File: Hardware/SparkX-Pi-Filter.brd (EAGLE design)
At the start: 25.4 x 25.4 mm, 19 parts

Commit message: Added Pi to 100 Digits
Added silk on back of board with Pi to 100 digits
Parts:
- added U$10: (no value), buzzard_labels_pi:50288419713
- added U$11: (no value), buzzard_labels_pi:69399375104
- added U$12: (no value), buzzard_labels_pi:58209749445
- added U$13: (no value), buzzard_labels_pi:59230781646
- added U$14: (no value), buzzard_labels_pi:06286208997
- added U$15: (no value), buzzard_labels_pi:86280348258
- added U$16: (no value), buzzard_labels_pi:34211706799
- added U$7: (no value), buzzard_labels_pi:3#4159265350
- added U$8: (no value), buzzard_labels_pi:89793238461
- added U$9: (no value), buzzard_labels_pi:26433832792
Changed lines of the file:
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@@
 <element name="U$5" library="buzzard_labels_v01" package="VIN1" value="" x="1.27" y="17.78" smashed="yes"/>
 <element name="U$6" library="buzzard_labels_v01" package="VOUT2" value="" x="19.05" y="17.78" smashed="yes"/>
+<element name="U$7" library="buzzard_labels_pi" package="3#4159265350" value="" x="17.78" y="24.13" smashed="yes" rot="MR0"/>
+<element name="U$8" library="buzzard_labels_pi" package="89793238461" value="" x="17.78" y="21.59" smashed="yes" rot="MR0"/>
+<element name="U$9" library="buzzard_labels_pi" package="26433832792" value="" x="17.78" y="19.05" smashed="yes" rot="MR0"/>
+<element name="U$10" library="buzzard_labels_pi" package="50288419713" value="" x="17.78" y="16.51" smashed="yes" rot="MR0"/>
+<element name="U$11" library="buzzard_labels_pi" package="69399375104" value="" x="17.78" y="13.97" smashed="yes" rot="MR0"/>
+<element name="U$12" library="buzzard_labels_pi" package="58209749445" value="" x="17.78" y="11.43" smashed="yes" rot="MR0"/>
+<element name="U$13" library="buzzard_labels_pi" package="59230781646" value="" x="17.78" y="8.89" smashed="yes" rot="MR0"/>
+<element name="U$14" library="buzzard_labels_pi" package="06286208997" value="" x="17.78" y="6.35" smashed="yes" rot="MR0"/>
+<element name="U$15" library="buzzard_labels_pi" package="86280348258" value="" x="17.78" y="3.81" smashed="yes" rot="MR0"/>
+<element name="U$16" library="buzzard_labels_pi" package="34211706799" value="" x="17.78" y="1.27" smashed="yes" rot="MR0"/>
 </elements>
 <signals>

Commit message: Changed Buzzard label for pi numbers to text
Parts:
- removed U$13: (no value), buzzard_labels_pi:59230781646
- removed U$14: (no value), buzzard_labels_pi:06286208997
- removed U$15: (no value), buzzard_labels_pi:86280348258
- removed U$16: (no value), buzzard_labels_pi:34211706799
- U$10: device buzzard_labels_pi:50288419713 -> buzzard_labels_pi_plaintext:0938446095_5058223172_53594081284
- U$11: device buzzard_labels_pi:69399375104 -> buzzard_labels_pi_plaintext:4811174502_8410270193_85211055595
- U$12: device buzzard_labels_pi:58209749445 -> buzzard_labels_pi_plaintext:6446229489_5493038196_44288109756
- U$6: device buzzard_labels_v01:VOUT2 -> buzzard_labels_pi_plaintext:3#1415926535__8979323846_26433832790
- U$7: device buzzard_labels_pi:3#4159265350 -> buzzard_labels_pi_plaintext:5028841971_6939937510_58209749441
- U$8: device buzzard_labels_pi:89793238461 -> buzzard_labels_pi_plaintext:5923078164_0628620899_86280348252
- U$9: device buzzard_labels_pi:26433832792 -> buzzard_labels_pi_plaintext:3421170679_8214808651_32823066473
- moved U$9 8.08 mm to (23.4, 13.2)
- moved U$11 7.74 mm to (22.9, 8.13)
- moved U$7 7.65 mm to (23.5, 19.1)
- moved U$10 7.22 mm to (23.4, 11.9)
- moved U$12 6.83 mm to (22.9, 6.86)
- moved U$8 6.76 mm to (23.4, 17.8)
- moved U$6 6.02 mm to (24.5, 20.3), flipped to the bottom
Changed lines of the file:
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@@
 <setting verticaltext="up"/>
 </settings>
-<grid distance="0.05" unitdist="inch" unit="inch" style="lines" multiple="1" display="yes" altdistance="0.005" altunitdist="inch" altunit="inch"/>
+<grid distance="0.01" unitdist="inch" unit="inch" style="lines" multiple="1" display="yes" altdistance="0.001" altunitdist="inch" altunit="inch"/>
 <layers>
 <layer number="1" name="Top" color="4" fill="1" visible="yes" active="yes"/>
@@
 <element name="U$4" library="buzzard_labels_v01" package="PI#FILTER3" value="" x="8.89" y="20.32" smashed="yes"/>
 <element name="U$5" library="buzzard_labels_v01" package="VIN1" value="" x="1.27" y="17.78" smashed="yes"/>
-<element name="U$6" library="buzzard_labels_v01" package="VOUT2" value="" x="19.05" y="17.78" smashed="yes"/>
-<element name="U$7" library="buzzard_labels_pi" package="3#4159265350" value="" x="17.78" y="24.13" smashed="yes" rot="MR0"/>
-<element name="U$8" library="buzzard_labels_pi" package="89793238461" value="" x="17.78" y="21.59" smashed="yes" rot="MR0"/>
-<element name="U$9" library="buzzard_labels_pi" package="26433832792" value="" x="17.78" y="19.05" smashed="yes" rot="MR0"/>
-<element name="U$10" library="buzzard_labels_pi" package="50288419713" value="" x="17.78" y="16.51" smashed="yes" rot="MR0"/>
-<element name="U$11" library="buzzard_labels_pi" package="69399375104" value="" x="17.78" y="13.97" smashed="yes" rot="MR0"/>
-<element name="U$12" library="buzzard_labels_pi" package="58209749445" value="" x="17.78" y="11.43" smashed="yes" rot="MR0"/>
-<element name="U$13" library="buzzard_labels_pi" package="59230781646" value="" x="17.78" y="8.89" smashed="yes" rot="MR0"/>
-<element name="U$14" library="buzzard_labels_pi" package="06286208997" value="" x="17.78" y="6.35" smashed="yes" rot="MR0"/>
-<element name="U$15" library="buzzard_labels_pi" package="86280348258" value="" x="17.78" y="3.81" smashed="yes" rot="MR0"/>
-<element name="U$16" library="buzzard_labels_pi" package="34211706799" value="" x="17.78" y="1.27" smashed="yes" rot="MR0"/>
+<element name="U$6" library="buzzard_labels_pi_plaintext" package="3#1415926535__8979323846_26433832790" value="" x="24.511" y="20.32" smashed="yes" rot="MR0"/>
+<element name="U$7" library="buzzard_labels_pi_plaintext" package="5028841971_6939937510_58209749441" value="" x="23.495" y="19.05" smashed="yes" rot="MR0"/>
+<element name="U$8" library="buzzard_labels_pi_plaintext" package="5923078164_0628620899_86280348252" value="" x="23.368" y="17.78" smashed="yes" rot="MR0"/>
+<element name="U$9" library="buzzard_labels_pi_plaintext" package="3421170679_8214808651_32823066473" value="" x="23.368" y="13.208" smashed="yes" rot="MR0"/>
+<element name="U$10" library="buzzard_labels_pi_plaintext" package="0938446095_5058223172_53594081284" value="" x="23.368" y="11.938" smashed="yes" rot="MR0"/>
+<element name="U$11" library="buzzard_labels_pi_plaintext" package="4811174502_8410270193_85211055595" value="" x="22.86" y="8.128" smashed="yes" rot="MR0"/>
+<element name="U$12" library="buzzard_labels_pi_plaintext" package="6446229489_5493038196_44288109756" value="" x="22.86" y="6.858" smashed="yes" rot="MR0"/>
 </elements>
 <signals>

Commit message: Updated to meet standards
Fixed width edge, added labels for C1, L1, C2 and Vout.  Added version.
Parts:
- added U$13: (no value), buzzard_labels_v01:VOUT2
- added U$14: (no value), buzzard_refdes_v01:C10
- added U$15: (no value), buzzard_refdes_v01:C21
- added U$16: (no value), buzzard_refdes_v01:L12
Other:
- board text added: "x01"
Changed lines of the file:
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@@
 <board>
 <plain>
-<wire x1="0" y1="0" x2="25.4" y2="0" width="0" layer="20"/>
-<wire x1="25.4" y1="0" x2="25.4" y2="25.4" width="0" layer="20"/>
-<wire x1="25.4" y1="25.4" x2="0" y2="25.4" width="0" layer="20"/>
-<wire x1="0" y1="25.4" x2="0" y2="0" width="0" layer="20"/>
+<wire x1="0" y1="0" x2="25.4" y2="0" width="0.2032" layer="20"/>
+<wire x1="25.4" y1="0" x2="25.4" y2="25.4" width="0.2032" layer="20"/>
+<wire x1="25.4" y1="25.4" x2="0" y2="25.4" width="0.2032" layer="20"/>
+<wire x1="0" y1="25.4" x2="0" y2="0" width="0.2032" layer="20"/>
 <text x="19.05" y="-17.78" size="1.778" layer="51" font="vector" ratio="15">The Hoff</text>
+<text x="9.144" y="1.016" size="1.778" layer="16" rot="MR0">x01</text>
 </plain>
 <attributes>
@@
 <element name="U$11" library="buzzard_labels_pi_plaintext" package="4811174502_8410270193_85211055595" value="" x="22.86" y="8.128" smashed="yes" rot="MR0"/>
 <element name="U$12" library="buzzard_labels_pi_plaintext" package="6446229489_5493038196_44288109756" value="" x="22.86" y="6.858" smashed="yes" rot="MR0"/>
+<element name="U$13" library="buzzard_labels_v01" package="VOUT2" value="" x="18.796" y="17.526" smashed="yes"/>
+<element name="U$14" library="buzzard_refdes_v01" package="C10" value="" x="3.556" y="12.7" smashed="yes"/>
+<element name="U$15" library="buzzard_refdes_v01" package="C21" value="" x="18.796" y="12.7" smashed="yes"/>
+<element name="U$16" library="buzzard_refdes_v01" package="L12" value="" x="11.176" y="17.018" smashed="yes"/>
 </elements>
 <signals>

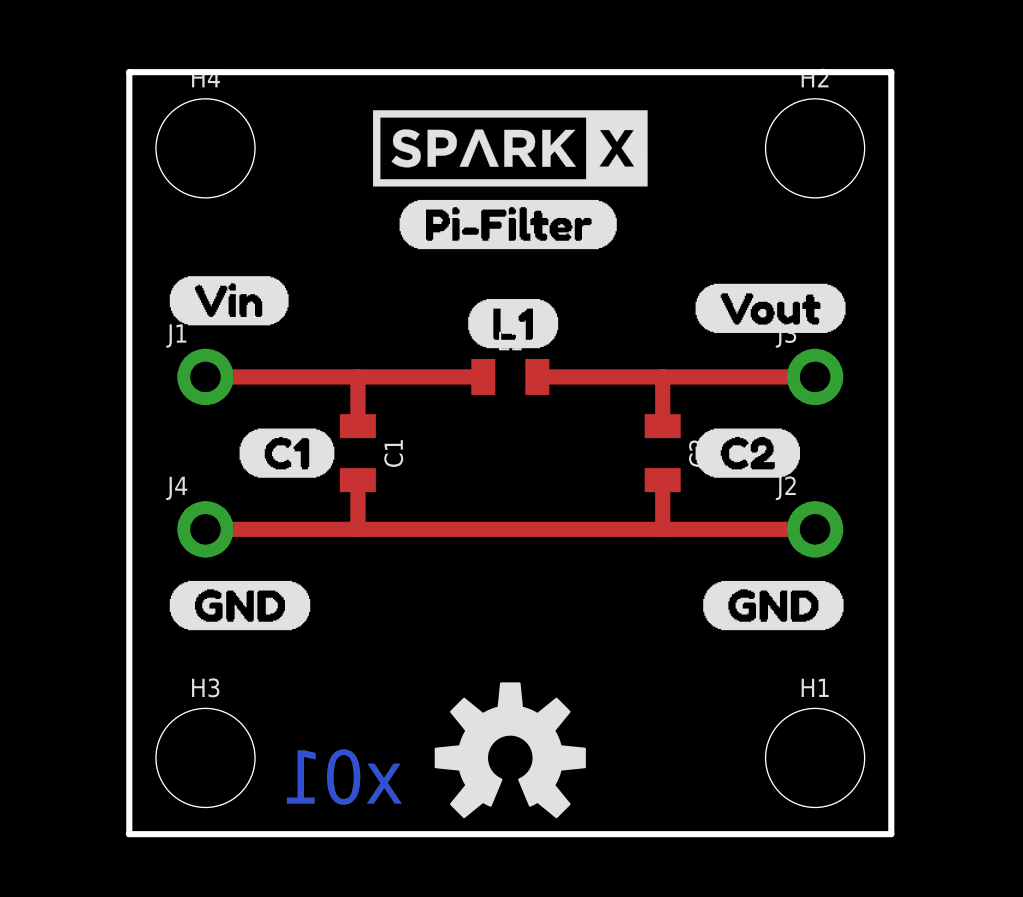
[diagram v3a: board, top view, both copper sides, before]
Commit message: Added Screw Terminals and adjusted labels
Added Screw Terminals and adjusted labels
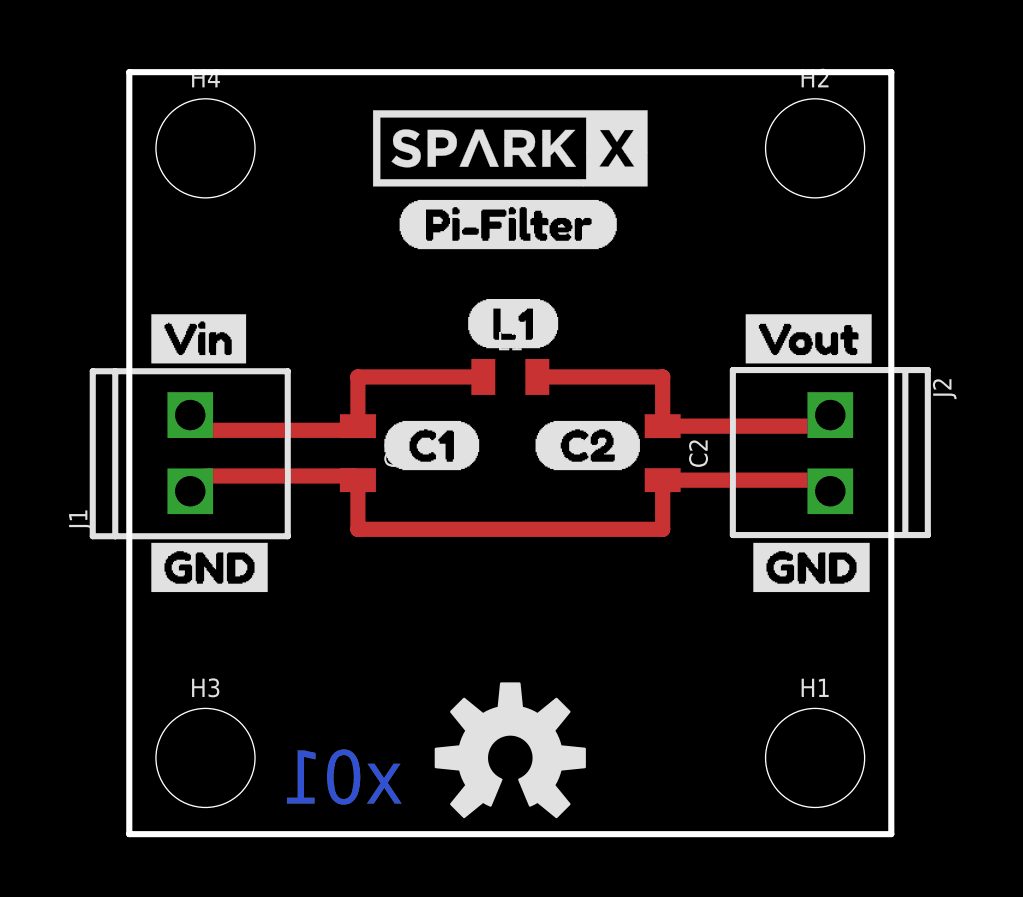
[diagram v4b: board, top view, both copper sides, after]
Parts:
- removed J3, J4: (no value), SparkFun-Connectors:1X01_NO_SILK
- J1, J2: device SparkFun-Connectors:1X01_NO_SILK -> SparkFun-Connectors:1X02_2.54_SCREWTERM
- U$13: device buzzard_labels_v01:VOUT2 -> buzzard_labels_v02:VOUT2
- U$2, U$3: device buzzard_labels_v01:GND0 -> buzzard_labels_v02:GND0
- U$5: device buzzard_labels_v01:VIN1 -> buzzard_labels_v02:VIN1
- moved U$2 19.1 mm to (20.3, 8.89)
- moved U$3 18.8 mm to (0.25, 8.89)
- moved U$15 5.34 mm to (13.5, 13.0)
- moved U$14 4.83 mm to (8.38, 13.0)
- moved J1 3.84 mm to (2.03, 11.4), turned to 90 degrees
- moved J2 3.84 mm to (23.4, 14.0), turned to 270 degrees
- moved U$5 1.63 mm to (0.25, 16.5)
- moved U$13 1.63 mm to (20.1, 16.5)
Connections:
- net GND: now also J1.P2, J2.P1; no longer J2.1, J4.1
- net N$1: now also J1.P1; no longer J1.1
- net N$2: now also J2.P2; no longer J3.1
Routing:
- net GND: track 23.6 -> 25.0 mm
- net N$1: track 10.9 -> 11.7 mm
- net N$2: track 10.9 -> 11.6 mm
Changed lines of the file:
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@@
 <attribute name="REV" value="x01" x="71.12" y="-19.05" size="1.778" layer="27" display="off"/>
-</element>
-<element name="J1" library="SparkFun-Connectors" package="1X01_NO_SILK" value="" x="2.54" y="15.24" smashed="yes">
-<attribute name="NAME" x="1.27" y="16.383" size="0.6096" layer="25" font="vector" ratio="20"/>
-<attribute name="VALUE" x="1.27" y="13.462" size="0.6096" layer="27" font="vector" ratio="20"/>
-</element>
-<element name="J2" library="SparkFun-Connectors" package="1X01_NO_SILK" value="" x="22.86" y="10.16" smashed="yes">
-<attribute name="NAME" x="21.59" y="11.303" size="0.6096" layer="25" font="vector" ratio="20"/>
-<attribute name="VALUE" x="21.59" y="8.382" size="0.6096" layer="27" font="vector" ratio="20"/>
-</element>
-<element name="J3" library="SparkFun-Connectors" package="1X01_NO_SILK" value="" x="22.86" y="15.24" smashed="yes">
-<attribute name="NAME" x="21.59" y="16.383" size="0.6096" layer="25" font="vector" ratio="20"/>
-<attribute name="VALUE" x="21.59" y="13.462" size="0.6096" layer="27" font="vector" ratio="20"/>
-</element>
-<element name="J4" library="SparkFun-Connectors" package="1X01_NO_SILK" value="" x="2.54" y="10.16" smashed="yes">
-<attribute name="NAME" x="1.27" y="11.303" size="0.6096" layer="25" font="vector" ratio="20"/>
-<attribute name="VALUE" x="1.27" y="8.382" size="0.6096" layer="27" font="vector" ratio="20"/>
 </element>
 <element name="L1" library="SparkFun-Coils" package="0805" value="DNP" x="12.7" y="15.24" smashed="yes">
@@
 <element name="U$1" library="SparkX" package="SPARKX-MEDIUM" value="SPARKX-LOGO4" x="12.7" y="22.86" smashed="yes"/>
 <element name="LOGO1" library="SparkFun-Aesthetics" package="OSHW-LOGO-M" value="OSHW-LOGOM" x="12.7" y="2.54" smashed="yes"/>
-<element name="U$2" library="buzzard_labels_v01" package="GND0" value="" x="1.27" y="7.62" smashed="yes"/>
-<element name="U$3" library="buzzard_labels_v01" package="GND0" value="" x="19.05" y="7.62" smashed="yes"/>
 <element name="U$4" library="buzzard_labels_v01" package="PI#FILTER3" value="" x="8.89" y="20.32" smashed="yes"/>
-<element name="U$5" library="buzzard_labels_v01" package="VIN1" value="" x="1.27" y="17.78" smashed="yes"/>
 <element name="U$6" library="buzzard_labels_pi_plaintext" package="3#1415926535__8979323846_26433832790" value="" x="24.511" y="20.32" smashed="yes" rot="MR0"/>
 <element name="U$7" library="buzzard_labels_pi_plaintext" package="5028841971_6939937510_58209749441" value="" x="23.495" y="19.05" smashed="yes" rot="MR0"/>
@@
 <element name="U$11" library="buzzard_labels_pi_plaintext" package="4811174502_8410270193_85211055595" value="" x="22.86" y="8.128" smashed="yes" rot="MR0"/>
 <element name="U$12" library="buzzard_labels_pi_plaintext" package="6446229489_5493038196_44288109756" value="" x="22.86" y="6.858" smashed="yes" rot="MR0"/>
-<element name="U$13" library="buzzard_labels_v01" package="VOUT2" value="" x="18.796" y="17.526" smashed="yes"/>
-<element name="U$14" library="buzzard_refdes_v01" package="C10" value="" x="3.556" y="12.7" smashed="yes"/>
-<element name="U$15" library="buzzard_refdes_v01" package="C21" value="" x="18.796" y="12.7" smashed="yes"/>
+<element name="U$14" library="buzzard_refdes_v01" package="C10" value="" x="8.382" y="12.954" smashed="yes"/>
+<element name="U$15" library="buzzard_refdes_v01" package="C21" value="" x="13.462" y="12.954" smashed="yes"/>
 <element name="U$16" library="buzzard_refdes_v01" package="L12" value="" x="11.176" y="17.018" smashed="yes"/>
+<element name="U$2" library="buzzard_labels_v02" package="GND0" value="" x="20.32" y="8.89" smashed="yes"/>
+<element name="U$3" library="buzzard_labels_v02" package="GND0" value="" x="0.254" y="8.89" smashed="yes"/>
+<element name="U$5" library="buzzard_labels_v02" package="VIN1" value="" x="0.254" y="16.51" smashed="yes"/>
+<element name="U$13" library="buzzard_labels_v02" package="VOUT2" value="" x="20.066" y="16.51" smashed="yes"/>
+<element name="J1" library="SparkFun-Connectors" package="1X02_2.54_SCREWTERM" value="" x="2.032" y="11.43" smashed="yes" rot="R90">
+<attribute name="NAME" x="-1.397" y="10.16" size="0.6096" layer="25" font="vector" ratio="20" rot="R90"/>
+<attribute name="VALUE" x="6.096" y="10.16" size="0.6096" layer="27" font="vector" ratio="20" rot="R90"/>
+</element>
+<element name="J2" library="SparkFun-Connectors" package="1X02_2.54_SCREWTERM" value="" x="23.368" y="13.97" smashed="yes" rot="R270">
+<attribute name="NAME" x="26.797" y="15.24" size="0.6096" layer="25" font="vector" ratio="20" rot="R270"/>
+<attribute name="VALUE" x="19.304" y="15.24" size="0.6096" layer="27" font="vector" ratio="20" rot="R270"/>
+</element>
 </elements>
 <signals>
@@
 <contactref element="C1" pad="1"/>
 <contactref element="L1" pad="1"/>
-<contactref element="J1" pad="1"/>
-<wire x1="2.54" y1="15.24" x2="7.62" y2="15.24" width="0.508" layer="1"/>
 <wire x1="7.62" y1="15.24" x2="11.8" y2="15.24" width="0.508" layer="1"/>
 <wire x1="7.62" y1="13.6" x2="7.62" y2="15.24" width="0.508" layer="1"/>
+<contactref element="J1" pad="P1"/>
+<wire x1="7.482" y1="13.462" x2="7.62" y2="13.6" width="0.508" layer="1" curve="90"/>
+<wire x1="2.032" y1="13.97" x2="2.54" y2="13.462" width="0.508" layer="1" curve="90"/>
+<wire x1="2.54" y1="13.462" x2="7.482" y2="13.462" width="0.508" layer="1"/>
 </signal>
 <signal name="N$2">
 <contactref element="L1" pad="2"/>
 <contactref element="C2" pad="1"/>
-<contactref element="J3" pad="1"/>
 <wire x1="13.6" y1="15.24" x2="17.78" y2="15.24" width="0.508" layer="1"/>
-<wire x1="17.78" y1="15.24" x2="22.86" y2="15.24" width="0.508" layer="1"/>
 <wire x1="17.78" y1="13.6" x2="17.78" y2="15.24" width="0.508" layer="1"/>
+<contactref element="J2" pad="P2"/>
+<wire x1="17.78" y1="13.6" x2="22.998" y2="13.6" width="0.508" layer="1"/>
+<wire x1="22.998" y1="13.6" x2="23.368" y2="13.97" width="0.508" layer="1"/>
 </signal>
 <signal name="GND">
 <contactref element="C1" pad="2"/>
-<contactref element="J2" pad="1"/>
 <contactref element="C2" pad="2"/>
-<contactref element="J4" pad="1"/>
 <wire x1="17.78" y1="11.8" x2="17.78" y2="10.16" width="0.508" layer="1"/>
-<wire x1="17.78" y1="10.16" x2="22.86" y2="10.16" width="0.508" layer="1"/>
 <wire x1="7.62" y1="11.8" x2="7.62" y2="10.16" width="0.508" layer="1"/>
-<wire x1="7.62" y1="10.16" x2="2.54" y2="10.16" width="0.508" layer="1"/>
 <wire x1="7.62" y1="10.16" x2="17.78" y2="10.16" width="0.508" layer="1"/>
 <polygon width="0.2032" layer="1" isolate="0.254">
@@
 <vertex x="0" y="25.4"/>
 </polygon>
+<contactref element="J1" pad="P2"/>
+<contactref element="J2" pad="P1"/>
+<wire x1="7.62" y1="11.8" x2="7.482" y2="11.938" width="0.508" layer="1" curve="90"/>
+<wire x1="2.54" y1="11.938" x2="2.032" y2="11.43" width="0.508" layer="1"/>
+<wire x1="7.482" y1="11.938" x2="2.54" y2="11.938" width="0.508" layer="1"/>
+<wire x1="17.78" y1="11.8" x2="22.998" y2="11.8" width="0.508" layer="1"/>
+<wire x1="22.998" y1="11.8" x2="23.368" y2="11.43" width="0.508" layer="1"/>
 </signal>
 </signals>
